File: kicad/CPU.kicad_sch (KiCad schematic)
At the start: 38 parts, among them SW1 SW_Push, U10 MC34063AD, U11 LD1117S33TR_SOT223, U5 STM32F303CBTx, X1 8 MHz

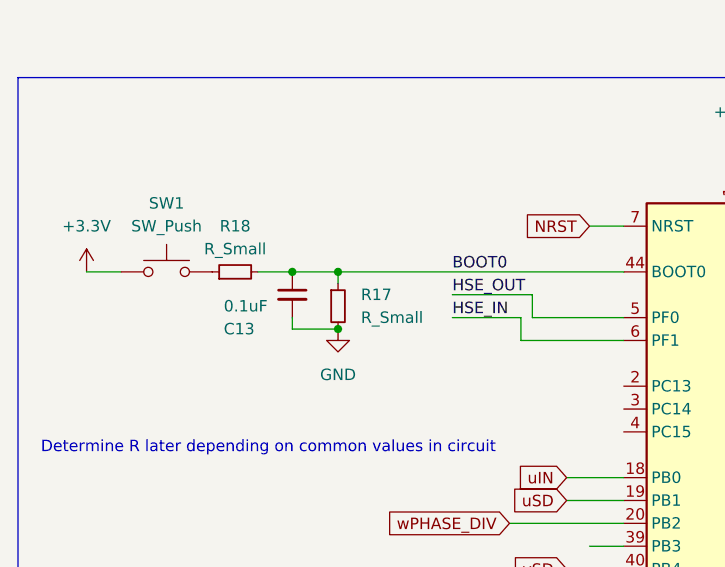
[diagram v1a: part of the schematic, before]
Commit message: [scripts] added simple debouncing circuit to driver, added rudimentary bootstrap circuit calculation, [simulations] Cleaned up filter simulations
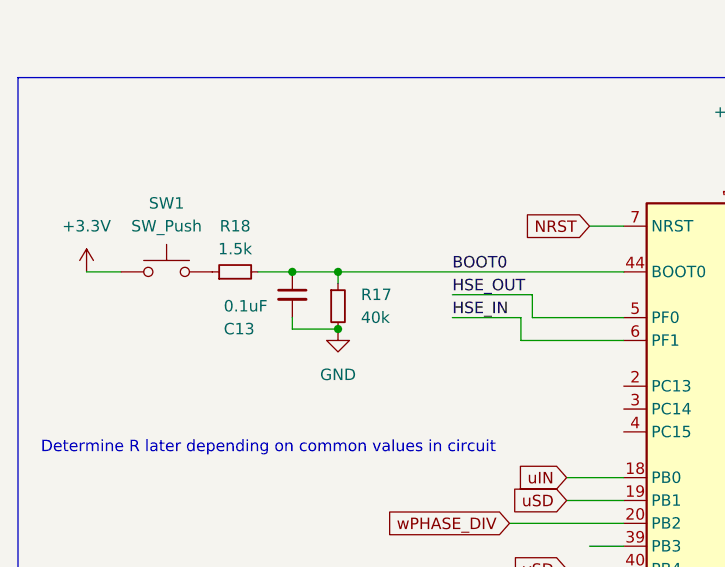
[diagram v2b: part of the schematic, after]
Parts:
- R17: value R_Small -> 40k
- R18: value R_Small -> 1.5k
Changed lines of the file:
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@@
       (effects (font (size 1.27 1.27)) (justify left))
     )
-    (property "Value" "R_Small" (at 52.07 123.19 0)
+    (property "Value" "40k" (at 52.07 123.19 0)
       (effects (font (size 1.27 1.27)) (justify left))
     )
@@
       (effects (font (size 1.27 1.27)))
     )
-    (property "Value" "R_Small" (at 38.1 115.57 90)
-      (effects (font (size 1.27 1.27)))
-    )
+    (property "Value" "1.5k" (at 38.1 115.57 90)
+      (effects (font (size 1.27 1.27)))
+    )

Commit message: [simulations] Added 10 V and 5 V simulations for buck converter, [scripts] Added bulk capacitor requirement notebook [kicad] Fixed buck converter schematic
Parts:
- C12: footprint (none) -> Capacitor_SMD:C_0603_1608Metric; JLCPCB (none) -> C19666
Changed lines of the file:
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@@
       (effects (font (size 1.27 1.27)) (justify left))
     )
-    (property "Footprint" "" (at 20.32 74.93 0)
+    (property "Footprint" "Capacitor_SMD:C_0603_1608Metric" (at 20.32 74.93 0)
       (effects (font (size 1.27 1.27)) hide)
     )
-    (property "Datasheet" "~" (at 20.32 74.93 0)
+    (property "Datasheet" "https://wmsc.lcsc.com/wmsc/upload/file/pdf/v2/lcsc/2304140030_Samsung-Electro-Mechanics-CL10A475KO8NNNC_C19666.pdf" (at 20.32 74.93 0)
       (effects (font (size 1.27 1.27)) hide)
     )
+    (property "JLCPCB" "C19666" (at 20.32 74.93 0)
+      (effects (font (size 1.27 1.27)) hide)
+    )

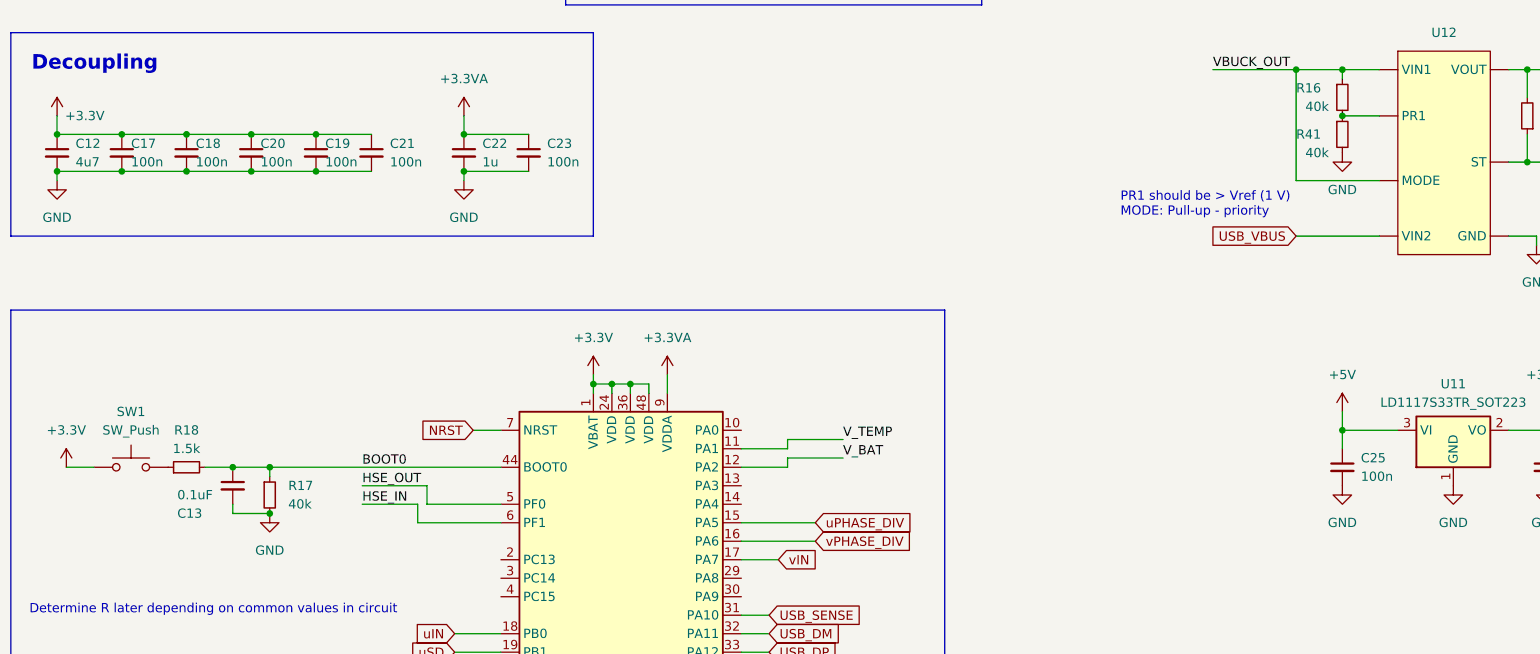
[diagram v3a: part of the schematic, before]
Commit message: [kicad] added component numbers from jlcpcb [scripts] added bulk capacitor plot
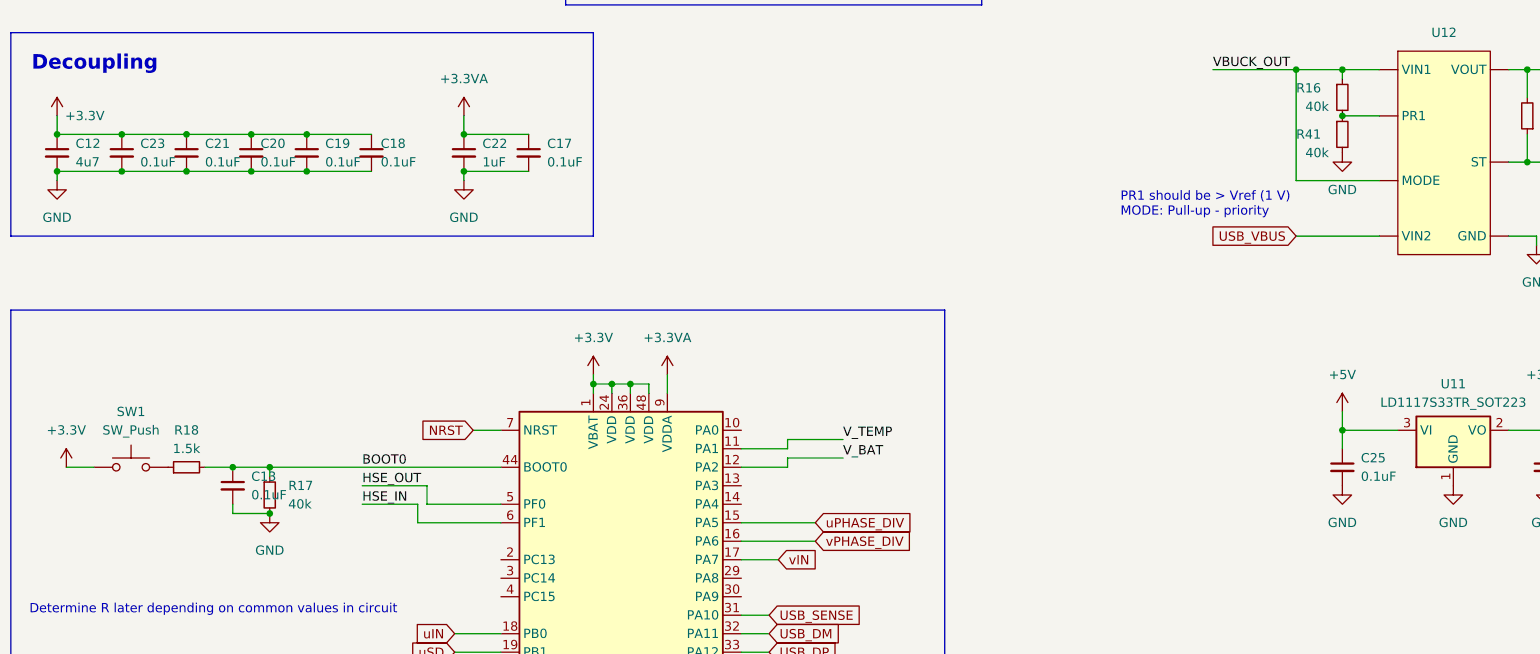
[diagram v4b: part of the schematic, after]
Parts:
- C13: footprint (none) -> Resistor_SMD:R_0402_1005Metric; jlcpcb (none) -> C307331
- C17, C18, C19, C20, C21, C23, C25: value 100n -> 0.1uF; footprint (none) -> Resistor_SMD:R_0402_1005Metric; jlcpcb (none) -> C307331
- C22: value 1u -> 1uF; footprint (none) -> Capacitor_SMD:C_1206_3216Metric; MFR.Part (none) -> CL31B105KBHNNNE; jlpcb (none) -> C1848
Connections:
- net +3.3V: now also C23.1; no longer C17.1
- net +3.3VA: now also C17.1; no longer C23.1

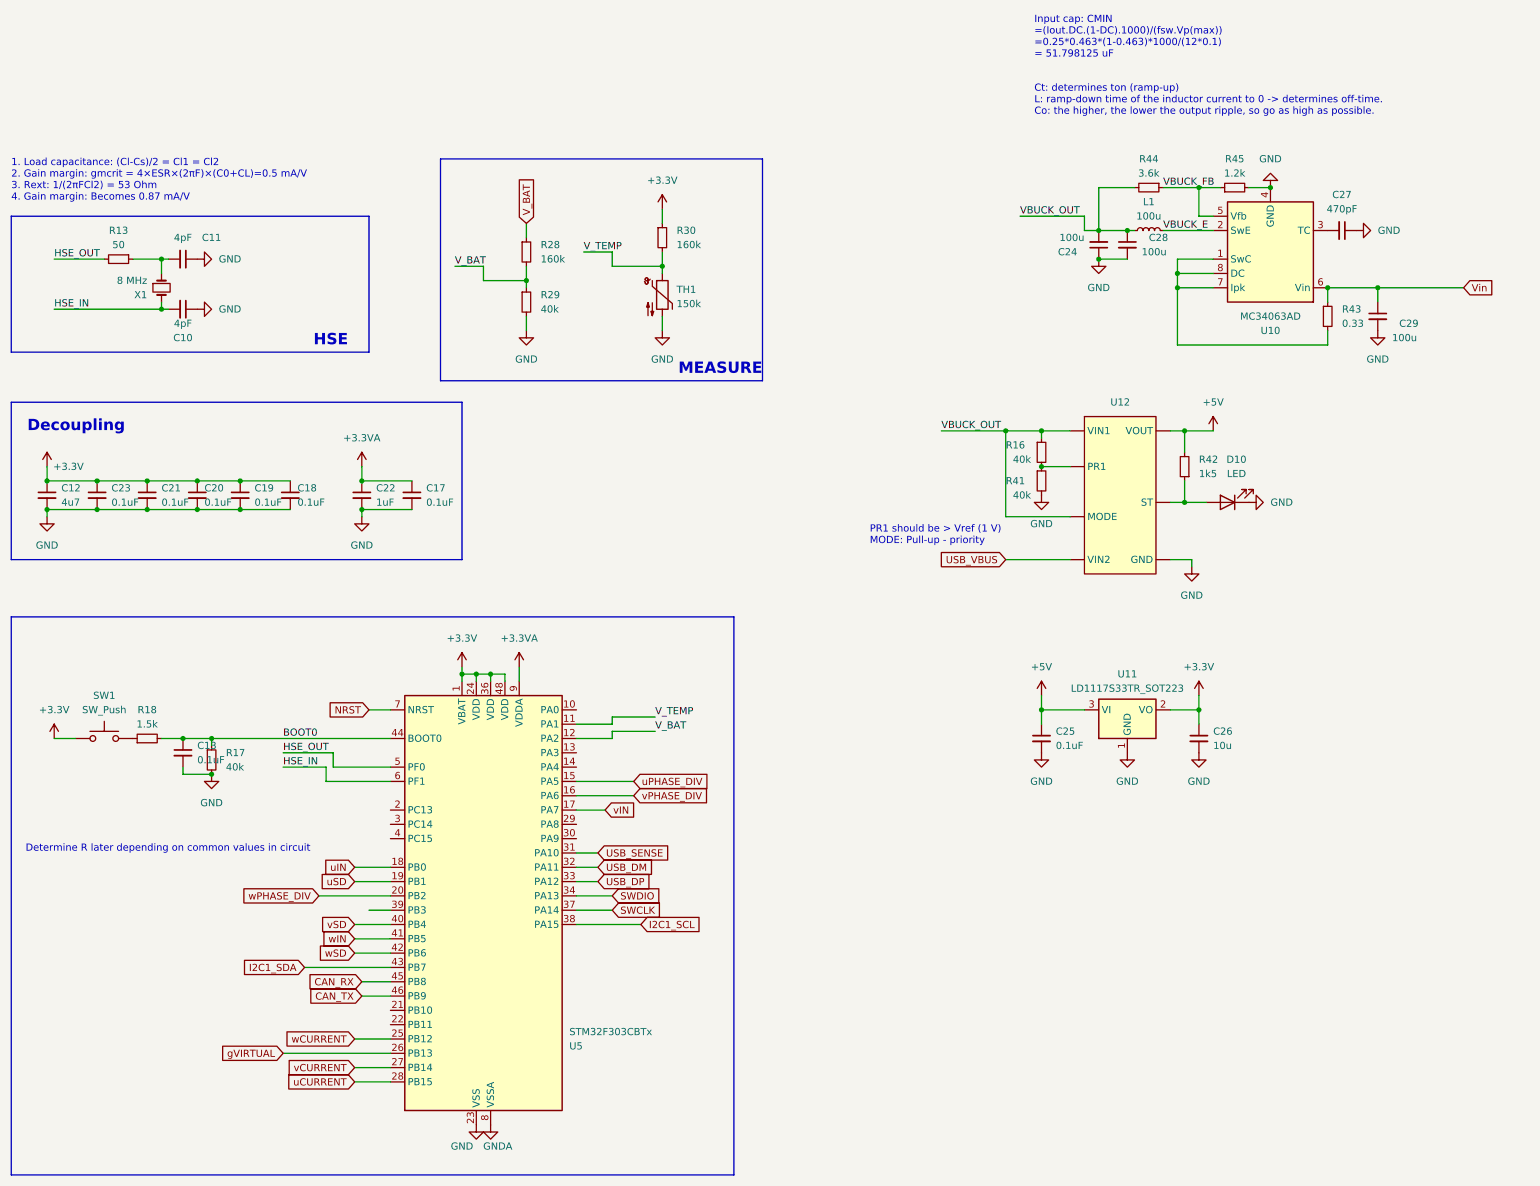
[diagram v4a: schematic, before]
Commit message: [kicad] Added resistor footprints and mfr numbers, added switching circuit for USB_DP, [simulations] Made switching circuit simulation
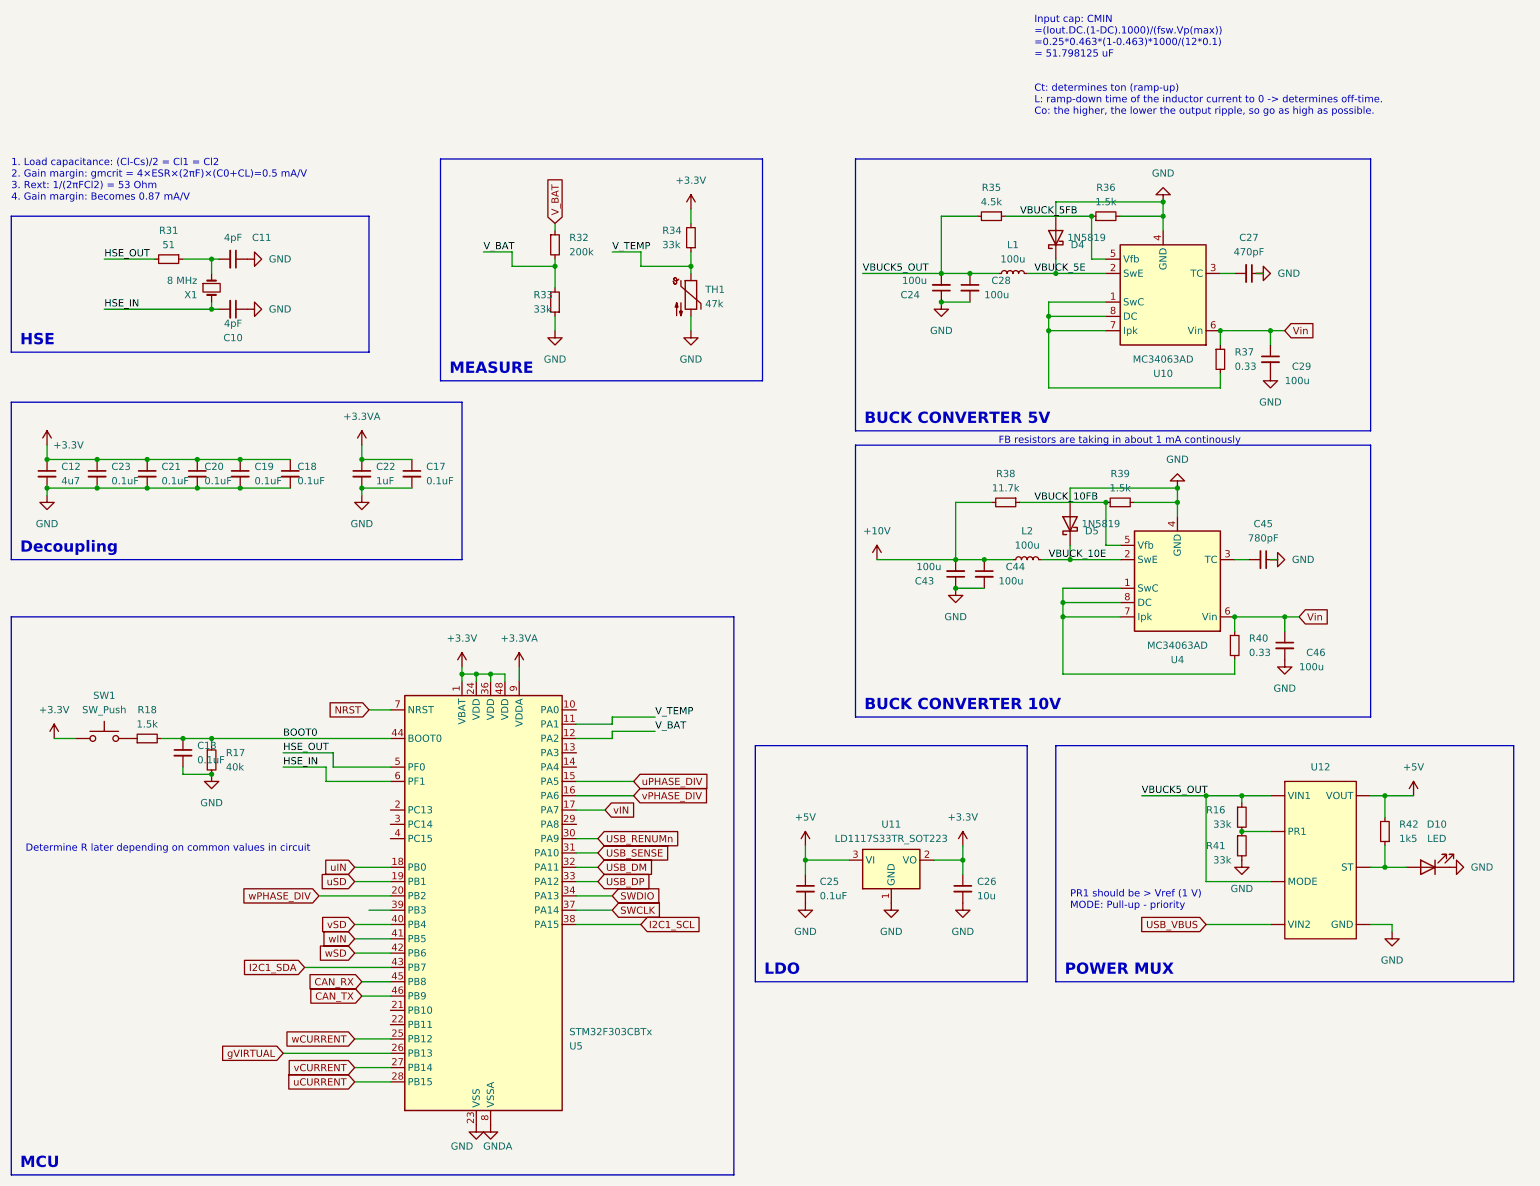
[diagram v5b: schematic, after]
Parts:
- removed R29: 40k, symbol Device:R_Small
- removed R30: 160k, symbol Device:R_Small
- added C43, C44, C46: 100u, Capacitor_SMD:C_1210_3225Metric, symbol Device:C_Small
- added C45: 780pF, Capacitor_SMD:C_0603_1608Metric, symbol Device:C_Small
- added D4, D5: 1N5819, Diode_THT:D_DO-41_SOD81_P10.16mm_Horizontal, symbol Diode:1N5819
- added L2: 100u, Inductor_SMD:L_1210_3225Metric, symbol Device:L_Small
- added R33, R34: 33k, Resistor_SMD:R_0603_1608Metric, symbol Device:R_Small
- added R38: 11.7k, symbol Device:R_Small
- added R39: 1.5k, symbol Device:R_Small
- added R40: 0.33, symbol Device:R_Small
- added U4: MC34063AD, Package_SO:SOIC-8_3.9x4.9mm_P1.27mm, symbol Regulator_Switching:MC34063AD
- R16, R41: value 40k -> 33k
- R31: renamed from R13; value 50 -> 51; footprint (none) -> Resistor_SMD:R_0805_2012Metric; MFR.PART (none) -> 0805W8F510JT5E; jlcpcb (none) -> C17738
- R32: renamed from R28; value 160k -> 200k; footprint (none) -> Resistor_SMD:R_0603_1608Metric; MFR.Part (none) -> 0603WAF2003T5E; jlcpcb (none) -> C25811
- R35: renamed from R44; value 3.6k -> 4.5k
- R36: renamed from R45; value 1.2k -> 1.5k
- TH1: value 150k -> 47k; MFR.Part (none) -> SDNT1005X473F4050FTF; Name MURATA NCP15WM154J03RC -> (none); jlcpcb (none) -> C279702
- renumbered R43 to R37
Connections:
- net +3.3V: now also R34.2
- net GND: now also C43.1, C44.2, C45.1, C46.2, D4.2 (A), D5.2 (A), R33.1, R39.2, U4.4 (GND)
- net V_BAT: now also R33.2
- net V_TEMP: now also R34.1
- net Vin: now also C46.1, R40.1, U4.6 (Vin)
- net USB_RENUMn: now reaches U5.30 (PA9)
- net VBUCK_E renamed VBUCK_5E
- net VBUCK_5E: now also D4.1 (K)
- net VBUCK_FB renamed VBUCK_5FB
- net VBUCK_OUT renamed VBUCK5_OUT
- new net: C45.2, U4.3 (TC)
- new net: R40.2, U4.1 (SwC), U4.7 (Ipk), U4.8 (DC)
- new net +10V: C43.2, C44.1, L2.1, R38.2
- new net VBUCK_10E: D5.1 (K), L2.2, U4.2 (SwE)
- new net VBUCK_10FB: R38.1, R39.1, U4.5 (Vfb)
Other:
- note added: "FB resistors are taking in about 1 mA continously"
- moved on the sheet: C10, C11, C12, C17, C18, C19, C20, C21, C22, C23, C24, C25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
